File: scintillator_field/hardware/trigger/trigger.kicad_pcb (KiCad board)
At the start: 2 copper layers, 110 parts, among them J1 Conn_02x03_Top_Bottom, J2 Conn_02x03_Top_Bottom, J3 A1, J4 A2, J5 A3, J6 Conn_Coaxial_Small, J7 Conn_02x03_Top_Bottom, J8 Conn_02x03_Top_Bottom, J9 Conn_Coaxial_Small, U1 LT3461A, U10 OPA855xDSG, U11 TLV3501AIDBV, U2 TPS7A4701, U3 TPS7A4701, U4 OPA855xDSG, U5 TLV3501AIDBV, U6 OPA855xDSG, U7 TLV3501AIDBV, U8 OPA855xDSG, U9 TLV3501AIDBV

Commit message: finalize pcb
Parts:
- added ?: , , F.Cu at (84.6, 83.2)
- added ?: , , F.Cu at (129.5, 85.0)
- added ?: , , F.Cu at (84.6, 117.8)
- added ?: , , F.Cu at (104.5, 85.0)
- added ?: , , F.Cu at (179.5, 85.0)
- added ?: , , F.Cu at (154.5, 85.0)
- added ?: , , F.Cu at (197.3, 89.5)
- added ?: , , F.Cu at (145.5, 115.0)
- added ?: , , F.Cu at (170.5, 115.0)
- added ?: , , F.Cu at (197.3, 112.3)
- added ?: , , F.Cu at (120.5, 115.0)
- added G***: LOGO, logos:sc, F.Cu at (192.5, 100.0)
- added G***: LOGO, logos:hep_14mm, B.Cu at (81.5, 95.5)
- added REF**: MountingHole_3.2mm_M3_DIN965_Pad, MountingHole:MountingHole_3.2mm_M3_DIN965_Pad, F.Cu at (95.5, 115.0)
- moved J9 95.0 mm to (188.5, 90.5), turned to 90 degrees
- moved J7 4.69 mm to (198.5, 85.0)
- moved J8 4.00 mm to (80.0, 84.5)
- moved J1 1.77 mm to (198.5, 119.0)
- moved J2 1.00 mm to (80.0, 119.0)
- moved +34.3V 0.40 mm to (85.1, 96.3)
- moved +3.8V 0.35 mm to (84.7, 110.8)
- moved R6 0.31 mm to (82.2, 97.4)
- moved C1 0.25 mm to (83.4, 96.8)
- renumbered TP5 to +2.1V, TP4 to +3.8V, TP2 to +33.1V, TP1 to +34.3V, TP3 to +5V
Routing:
- net +5V: track 9.27 -> 178.4 mm, vias 2 -> 10
- net +2.1V: track 7.08 -> 124.9 mm, vias 4 -> 8
- net +3.8V: track 4.48 -> 116.4 mm, vias 0 -> 5
- net +33.1V: track 0.00 -> 103.3 mm
- net /amplifiers/DOUT1: track 3.38 -> 88.6 mm
- net /amplifiers/DOUT2: track 3.38 -> 60.9 mm
- net /amplifiers/DOUT3: track 3.40 -> 35.9 mm
- net /amplifiers/DOUT4: track 3.26 -> 11.2 mm
- net GND: track 0.00 -> 0.49 mm, vias 0 -> 195
- added copper zone on B.Cu, net GND
- added copper zone on F.Cu, net GND
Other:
- board outline added: 128.5 x 42 mm
- board text added: "+5V"
- board text added: "ALEX X ENRICHED P&E 2025/03/16"
- board text added: "D1"
- board text added: "D2"
- board text added: "D3"
- board text added: "D3 D4 +5V D2 D1 GND"
- board text added: "D4"
- board text added: "GND"

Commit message: fix trigger pcb
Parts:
- added J10: Conn_Coaxial_Small, connectors:BWIPX-1-001E, F.Cu at (102.0, 116.0)
- added J11: Conn_Coaxial_Small, connectors:BWIPX-1-001E, F.Cu at (127.0, 116.0)
- added J12: Conn_Coaxial_Small, connectors:BWIPX-1-001E, F.Cu at (152.0, 116.0)
- added J13: Conn_Coaxial_Small, connectors:BWIPX-1-001E, F.Cu at (177.0, 116.0)
- C1: value 1.6p -> 22p
- C2, C3, C4, C45, C6, C8: footprint Capacitor_SMD:C_0402_1005Metric -> Capacitor_SMD:C_0603_1608Metric
- C25, C34, C43, C44: value 5p -> 3p
- J3: value A1 -> Conn_Coaxial_Small
- J4: value A2 -> Conn_Coaxial_Small
- J5: value A3 -> Conn_Coaxial_Small
- moved C45 7.06 mm to (75.0, 103.2), turned to 0 degrees
- moved C46 6.29 mm to (74.5, 102.0), turned to 0 degrees
- moved C2 4.53 mm to (82.2, 98.6), turned to -90 degrees
- moved C1 2.43 mm to (84.8, 98.8)
- moved R6 1.93 mm to (83.7, 98.6)
- moved C3 0.57 mm to (84.4, 94.0)
- moved C6 0.56 mm to (77.2, 110.7)
- moved +5V0 0.43 mm to (75.0, 109.8)
- moved C8 0.39 mm to (75.1, 105.8)
- moved C4 0.25 mm to (79.5, 95.8)
- moved R5 0.12 mm to (80.2, 102.0)
- renumbered +2.1V to +1V2, +33.1V to +33V1, +34.3V to +34V3, +3.8V to +3V8, +5V to +5V0
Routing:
- net /amplifiers/DOUT1: track 88.6 -> 99.1 mm
- net /amplifiers/DOUT2: track 60.9 -> 71.4 mm
- net /amplifiers/DOUT3: track 35.9 -> 46.3 mm
- net /amplifiers/DOUT4: track 11.2 -> 21.5 mm
- net +5V: track 178.4 -> 182.0 mm, vias 10 -> 12
- net (no net): track 0.00 -> 1.28 mm
- net GND: track 0.49 -> 1.15 mm, vias 195 -> 200

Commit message: fix trigger pcb
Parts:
- G***: moved to F.Cu
- moved G*** 52.7 mm to (142.0, 85.0)
- moved G*** 37.0 mm to (117.0, 85.0), turned to 0 degrees
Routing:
- net GND: vias 200 -> 203
- net +2.1V: vias 8 -> 5

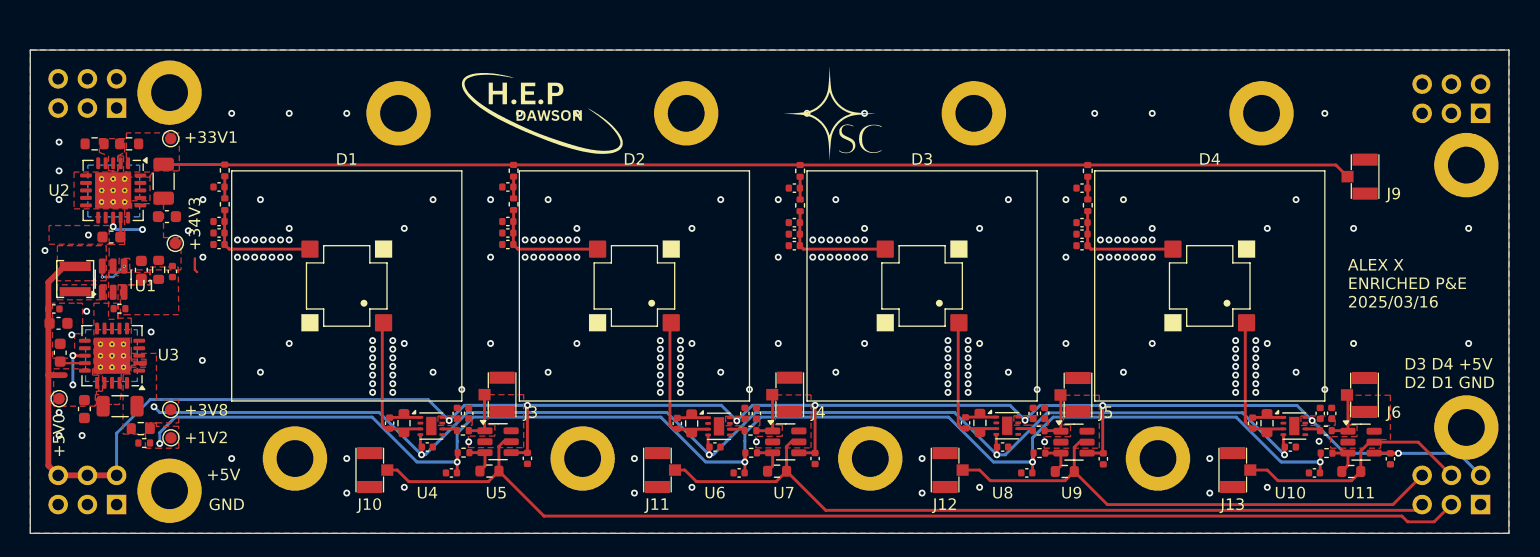
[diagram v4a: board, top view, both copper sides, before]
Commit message: update to opa858
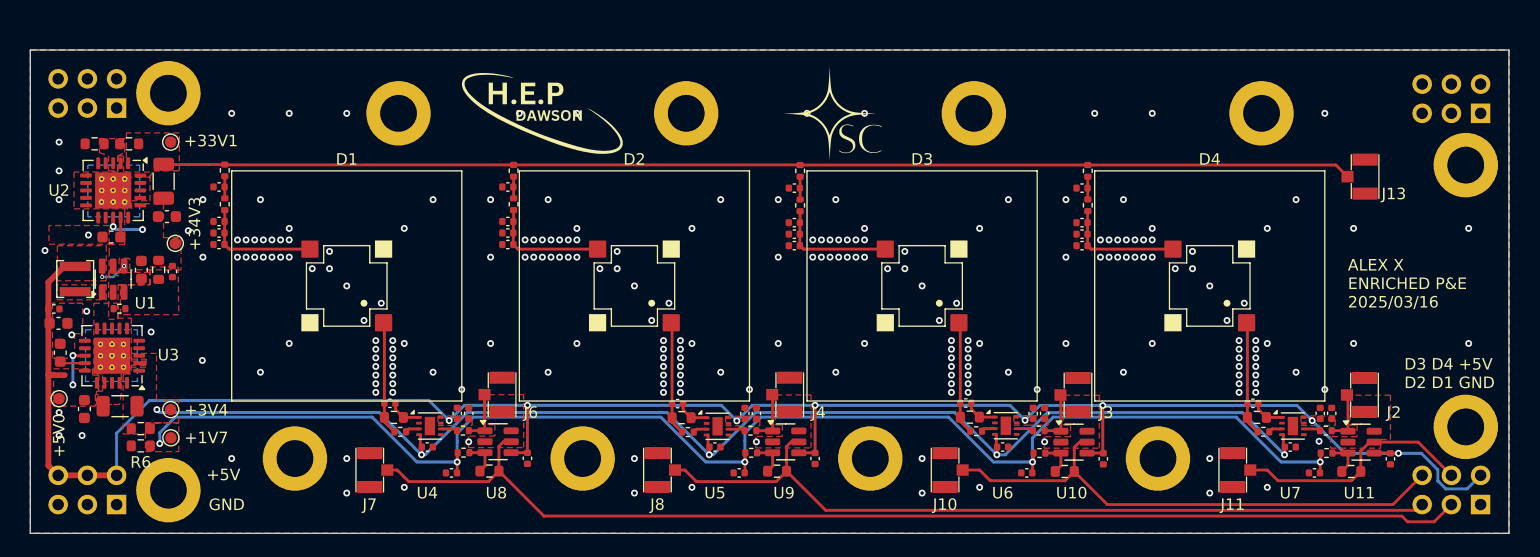
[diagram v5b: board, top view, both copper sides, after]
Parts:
- removed ? (x11): , 
- removed the C34 at (128.7, 112.0)
- removed the C43 at (153.8, 111.9)
- removed the C44 at (178.7, 111.9)
- removed the R10 at (82.4, 113.7)
- removed the R26 at (130.0, 112.0)
- removed the R30 at (155.0, 111.9)
- removed the R34 at (180.0, 111.9)
- removed REF**: MountingHole_3.2mm_M3_DIN965_Pad, MountingHole:MountingHole_3.2mm_M3_DIN965_Pad
- removed the U10 at (182.3, 112.2)
- removed the U8 at (157.4, 112.2)
- added C28: 3p, Capacitor_SMD:C_0402_1005Metric, F.Cu at (128.8, 110.2)
- added C29: 3p, Capacitor_SMD:C_0402_1005Metric, F.Cu at (153.8, 110.2)
- added C30: 3p, Capacitor_SMD:C_0402_1005Metric, F.Cu at (178.8, 110.2)
- added H1: M3, MountingHole:MountingHole_3.2mm_M3_DIN965_Pad, F.Cu at (104.5, 85.0)
- added H10: M3, MountingHole:MountingHole_3.2mm_M3_DIN965_Pad, F.Cu at (84.5, 117.8)
- added H11: M3, MountingHole:MountingHole_3.2mm_M3_DIN965_Pad, F.Cu at (197.2, 89.5)
- added H12: M3, MountingHole:MountingHole_3.2mm_M3_DIN965_Pad, F.Cu at (197.2, 112.2)
- added H2: M3, MountingHole:MountingHole_3.2mm_M3_DIN965_Pad, F.Cu at (95.5, 115.0)
- added H3: M3, MountingHole:MountingHole_3.2mm_M3_DIN965_Pad, F.Cu at (129.5, 85.0)
- added H4: M3, MountingHole:MountingHole_3.2mm_M3_DIN965_Pad, F.Cu at (120.5, 115.0)
- added H5: M3, MountingHole:MountingHole_3.2mm_M3_DIN965_Pad, F.Cu at (154.5, 85.0)
- added H6: M3, MountingHole:MountingHole_3.2mm_M3_DIN965_Pad, F.Cu at (145.5, 115.0)
- added H7: M3, MountingHole:MountingHole_3.2mm_M3_DIN965_Pad, F.Cu at (179.5, 85.0)
- added H8: M3, MountingHole:MountingHole_3.2mm_M3_DIN965_Pad, F.Cu at (170.5, 115.0)
- added H9: M3, MountingHole:MountingHole_3.2mm_M3_DIN965_Pad, F.Cu at (84.5, 83.2)
- added R15: 20R, Resistor_SMD:R_0402_1005Metric, F.Cu at (104.7, 112.7)
- added R16: 20R, Resistor_SMD:R_0402_1005Metric, F.Cu at (129.7, 112.7)
- added R17: 20R, Resistor_SMD:R_0402_1005Metric, F.Cu at (154.7, 112.6)
- added R18: 20R, Resistor_SMD:R_0402_1005Metric, F.Cu at (179.7, 112.7)
- added R20: 226k 0.1%, Resistor_SMD:R_0603_1608Metric, F.Cu at (129.1, 111.5)
- added R21: 226k 0.1%, Resistor_SMD:R_0603_1608Metric, F.Cu at (154.2, 111.4)
- added R22: 226k 0.1%, Resistor_SMD:R_0603_1608Metric, F.Cu at (179.1, 111.4)
- added R6: 10k 0.1%, Resistor_SMD:R_0603_1608Metric, F.Cu at (82.1, 113.9)
- added U5: OPA858xDSG, Package_SON:WSON-8-1EP_2x2mm_P0.5mm_EP0.9x1.6mm, F.Cu at (132.2, 112.2)
- added U7: OPA858xDSG, Package_SON:WSON-8-1EP_2x2mm_P0.5mm_EP0.9x1.6mm, F.Cu at (182.2, 112.2)
- U4, U6: value OPA855xDSG -> OPA858xDSG
- moved U6 24.9 mm to (157.3, 112.2)
- moved C27 1.73 mm to (103.8, 110.2), turned to 0 degrees
- moved R19 1.01 mm to (104.1, 111.4), turned to 0 degrees
- moved +33V1 0.30 mm to (84.7, 87.5)
- moved U4 0.12 mm to (107.2, 112.2)
- renumbered +1V2 to +1V7, +3V8 to +3V4, C7 to C10, C9 to C11, C13 to C12, C17 to C13, C21 to C14, C10 to C15, C14 to C16, C18 to C17, C22 to C18, C11 to C19, C46 to C2, C15 to C20, C19 to C21, C23 to C22, C12 to C23, C16 to C24, C20 to C25, C24 to C26, C25 to C27, C45 to C3, C26 to C31, C35 to C32, C27 to C33, C36 to C34, C28 to C35, C37 to C36, C29 to C37, C47 to C39, C2 to C4, C49 to C40, C30 to C41, C39 to C42, C31 to C43, C40 to C44, C32 to C45, C41 to C46, C33 to C47, C42 to C48, C48 to C49, C3 to C5, C4 to C6, C5 to C7, C6 to C8, C8 to C9, J7 to J1, J12 to J10, J13 to J11, J1 to J12, J9 to J13, J6 to J2, J5 to J3, J8 to J5, J3 to J6, J10 to J7, J11 to J8, J2 to J9, R5 to R1, R17 to R10, R12 to R11, R14 to R12, R16 to R13, R18 to R14, R22 to R19, R6 to R2, R21 to R23, R25 to R24, R29 to R25, R33 to R26, R19 to R27, R23 to R28, R27 to R29, R7 to R3, R31 to R30, R20 to R31, R24 to R32, R28 to R33, R32 to R34, R8 to R4, R9 to R5, R11 to R7, R13 to R8, R15 to R9, U9 to U10, U5 to U8, U7 to U9
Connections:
- net +2.1V renamed +1.7V
- net +3.8V renamed +3.4V
- R24 pad 1: Net-(R25-Pad1) -> Net-(R24-Pad1)
- R25 pad 1: Net-(R29-Pad1) -> Net-(R25-Pad1)
- U3 pad 10: unconnected-(U3-0.4V-Pad10) -> GND
- U3 pad 9: GND -> unconnected-(U3-0.8V-Pad9)
- U4 pad 3: /amplifiers/IN1 -> Net-(U4--)
- U6 pad 3: /amplifiers/IN2 -> Net-(U6--)
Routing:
- net Net-(U5-FB): track 0.00 -> 2.86 mm
- net Net-(U7-FB): track 0.00 -> 2.86 mm
- net Net-(U10-FB): track 2.68 -> 0.00 mm
- net Net-(U8-FB): track 2.68 -> 0.00 mm
- net /amplifiers/IN4: track 12.5 -> 10.0 mm
- net /amplifiers/IN3: track 12.3 -> 9.92 mm
- net /amplifiers/IN1: track 12.4 -> 10.0 mm
- net /amplifiers/IN2: track 12.4 -> 10.0 mm
- net Net-(R29-Pad1): track 1.35 -> 0.00 mm
- net Net-(R24-Pad1): track 0.00 -> 1.33 mm
- net (no net): track 1.28 -> 0.00 mm
- net Net-(U5--): track 0.00 -> 1.22 mm
- net Net-(U4--): track 0.00 -> 1.22 mm
- net Net-(U7--): track 0.00 -> 1.21 mm
- net Net-(U6--): track 0.00 -> 1.21 mm
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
